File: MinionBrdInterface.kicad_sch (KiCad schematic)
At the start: 4 parts, among them J30 Backup Camera, J5 MinionConn, J6 SPI, SW1 BACKUP_SW

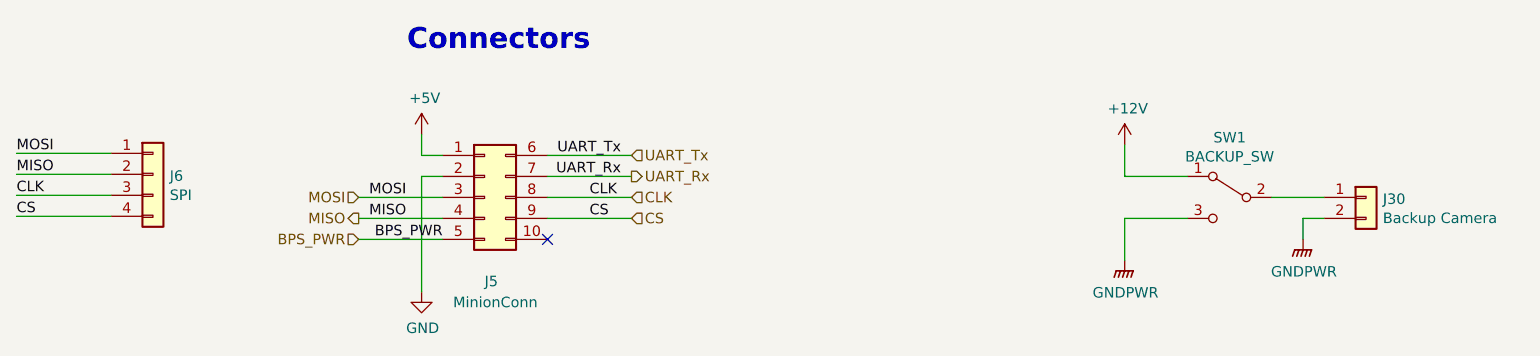
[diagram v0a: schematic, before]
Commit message: Schematic notations for rework changes
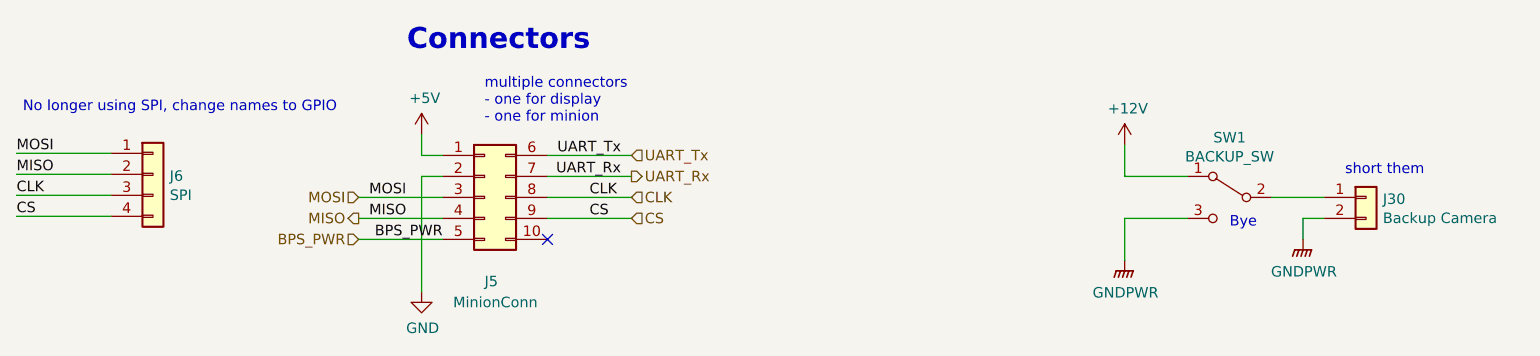
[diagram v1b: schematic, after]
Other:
- note added: "Bye"
- note added: "No longer using SPI, change names to GPIO"
- note added: "multiple connectors - one for display - one for minion"
- note added: "short them"

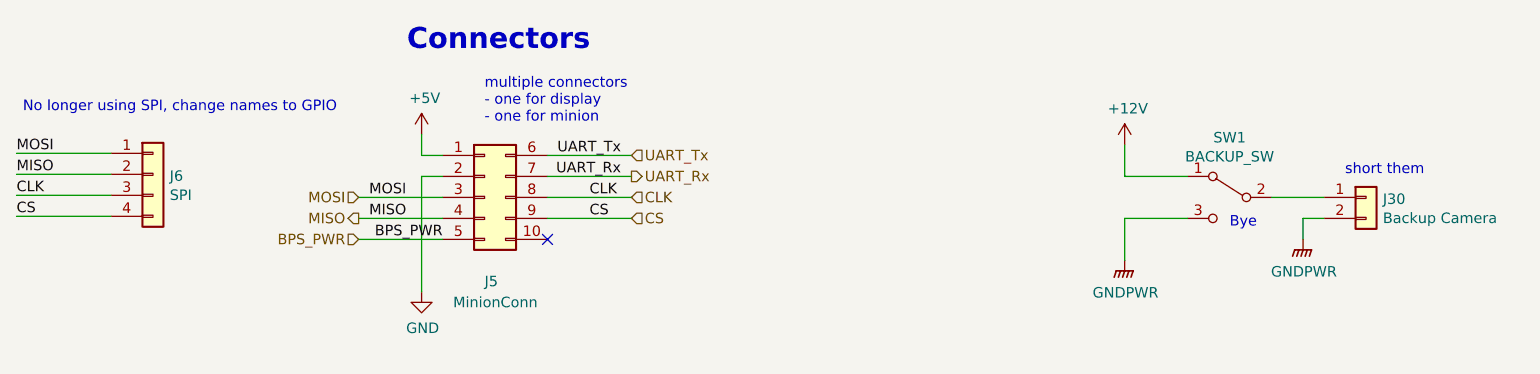
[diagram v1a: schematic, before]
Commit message: Updated schematic in accordance to previous weeks annotated changes
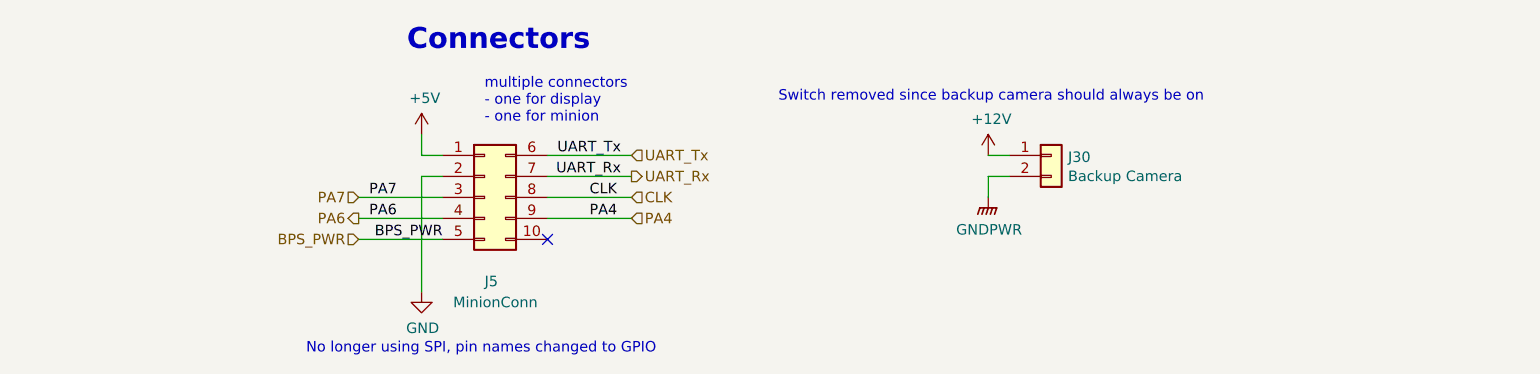
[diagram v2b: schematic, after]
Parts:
- removed J6: SPI, Connector_PinHeader_2.54mm:PinHeader_1x04_P2.54mm_Vertical, symbol Connector_Generic:Conn_01x04
- removed SW1: BACKUP_SW, Connector_Molex:Molex_Micro-Fit_3.0_43650-0315_1x03_P3.00mm_Vertical, symbol Switch:SW_SPDT
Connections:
- net +12V: now also J30.1 (Pin_1)
- net CS renamed PA4
- net MISO renamed PA6
- net MOSI renamed PA7
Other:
- note added: "No longer using SPI, pin names changed to GPIO"
- note added: "Switch removed since backup camera should always be on"
- note removed: "Bye"
- note removed: "No longer using SPI, change names to GPIO"
- note removed: "short them"
- moved on the sheet: J30

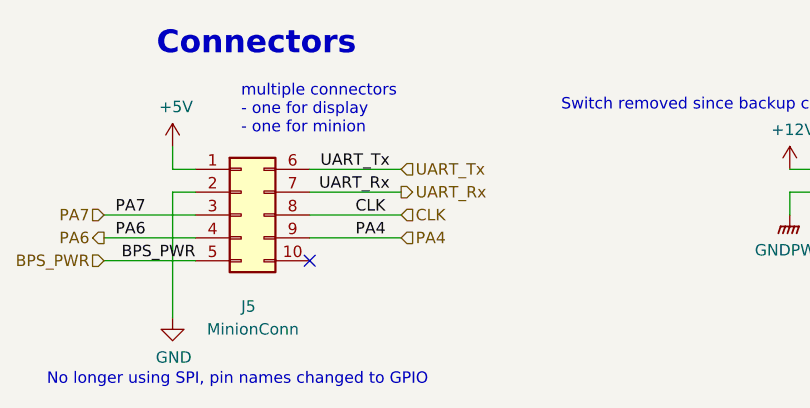
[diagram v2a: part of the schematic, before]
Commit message: Renamed Clk to PA5, removed CAN_TX/RX test points, deleted other .lck file and #auto_saved_files# (hopefully this does not break anything.
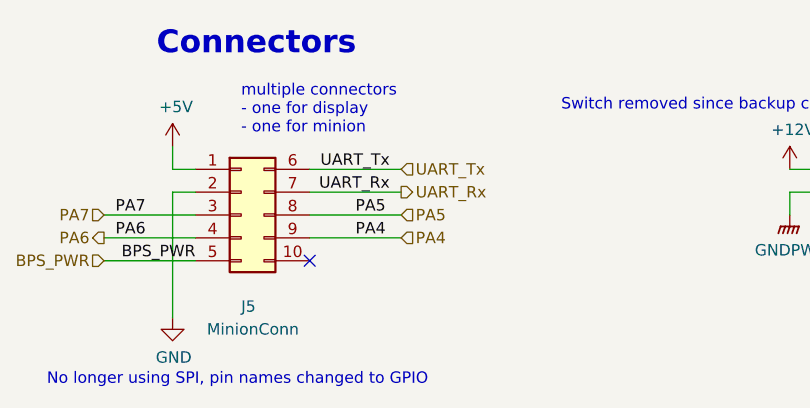
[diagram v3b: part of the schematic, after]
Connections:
- net CLK renamed PA5

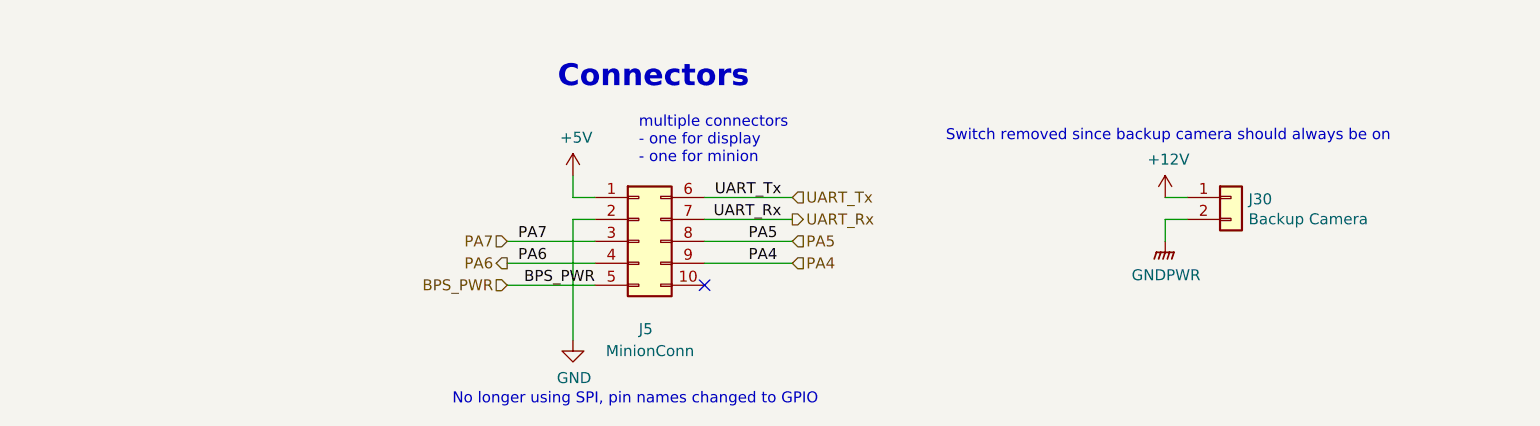
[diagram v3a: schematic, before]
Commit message: removed camera, fixed connectors, and changed status LEDS
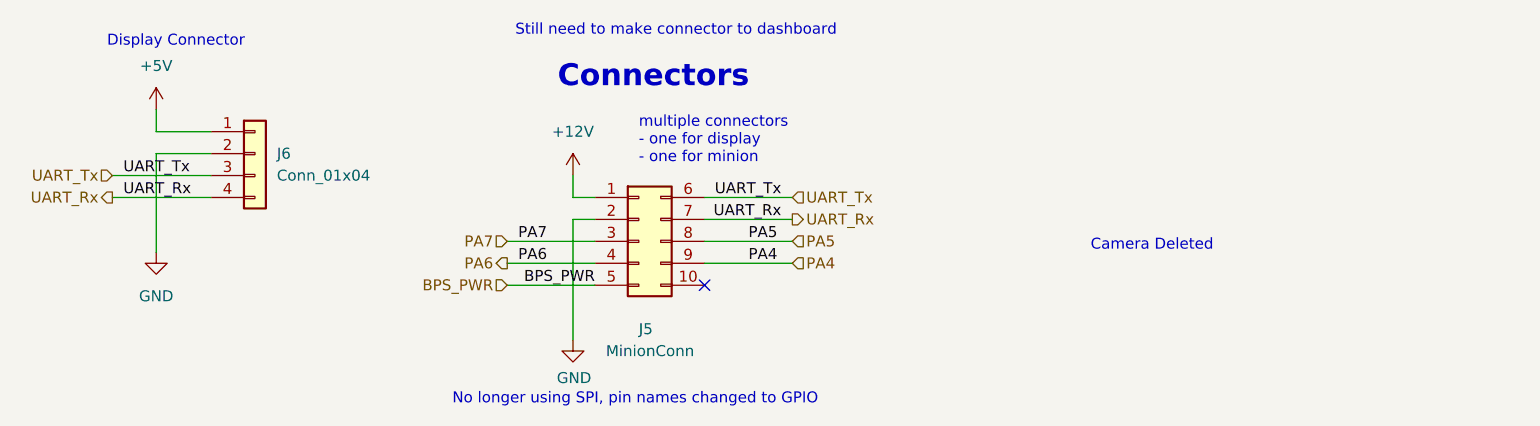
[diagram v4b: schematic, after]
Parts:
- removed J30: Backup Camera, Connector_Molex:Molex_Micro-Fit_3.0_43650-0215_1x02_P3.00mm_Vertical, symbol Connector_Generic:Conn_01x02
- added J6: Conn_01x04, Connector_Molex:Molex_Micro-Fit_3.0_43650-0415_1x04_P3.00mm_Vertical, symbol Connector_Generic:Conn_01x04
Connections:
- net +12V: now also J5.1 (Pin_1)
- net +5V: now also J6.1 (Pin_1); no longer J5.1 (Pin_1)
- net GND: now also J6.2 (Pin_2)
- net UART_Rx: now also J6.4 (Pin_4)
- net UART_Tx: now also J6.3 (Pin_3)
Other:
- note added: "Camera Deleted"
- note added: "Display Connector"
- note added: "Still need to make connector to dashboard"
- note removed: "Switch removed since backup camera should always be on"

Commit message: Schematic finished :) hopefully not broken
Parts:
- removed J5: MinionConn, Connector_Molex:Molex_Micro-Fit_3.0_43045-1012_2x05_P3.00mm_Vertical, symbol Connector_Generic:Conn_02x05_Top_Bottom
- added J4: Conn_02x05_Top_Bottom, symbol Connector_Generic:Conn_02x05_Top_Bottom
- added R10, R11, R12, R30, R33, R40, R5, R6: 4.9k, Resistor_SMD:R_0805_2012Metric, symbol Device:R_US
- added R32, R39, R41, R43, R45, R47, R49, R51: 510, Resistor_SMD:R_0805_2012Metric, symbol Device:R_US
- added U1, U16, U2, U20, U21, U22, U3, U4: EL3H7, Package_SO:SOP-4_4.4x2.6mm_P1.27mm, symbol Isolator:SFH617A-1
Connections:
- net +12V: now also J4.1 (Pin_1), U22.3
- net GND: now also R10.2, R11.2, R12.2, R30.2, R33.2, R5.2, R6.2, U22.2
- new net: R45.2, U16.1
- new net: R51.2, U22.1
- new net: R49.2, U21.1
- new net: R39.2, U2.1
- new net: R41.2, U3.1
- new net: R32.2, U1.1
- new net: R47.2, U20.1
- new net: R43.2, U4.1
- new net +3.3V: U1.3, U16.3, U2.3, U20.3, U21.3, U3.3, U4.3
- new net Cruise_En: J4.7 (Pin_7), R12.1, R47.1, U20.4
- new net Cruise_Set: J4.6 (Pin_6), R30.1, R49.1, U21.4
- new net Forward_Gear: J4.8 (Pin_8), R45.1
- new net Foward_Gear: R11.1, U16.4
- new net GNDPWR: J4.5 (Pin_5), R40.2, U1.2, U16.2, U2.2, U20.2, U21.2, U3.2, U4.2
- new net Heartbeat: J4.10 (Pin_10), R40.1, R51.1, U22.4
- new net IGN_1(Array): J4.3 (Pin_3), R33.1, R39.1, U2.4
- new net IGN_2(Motor): J4.4 (Pin_4), R32.1, R5.1, U1.4
- new net Regen: J4.2 (Pin_2), R41.1, R6.1, U3.4
- new net Reverse_Gear: J4.9 (Pin_9), R10.1, R43.1, U4.4
- no-connect marks 1 -> 0
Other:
- note added: "Connectors + Optoisolators"
- note removed: "Camera Deleted"
- note removed: "Connectors"
- note removed: "No longer using SPI, pin names changed to GPIO"
- note removed: "Still need to make connector to dashboard"
- note removed: "multiple connectors - one for display - one for minion"
- moved on the sheet: J6

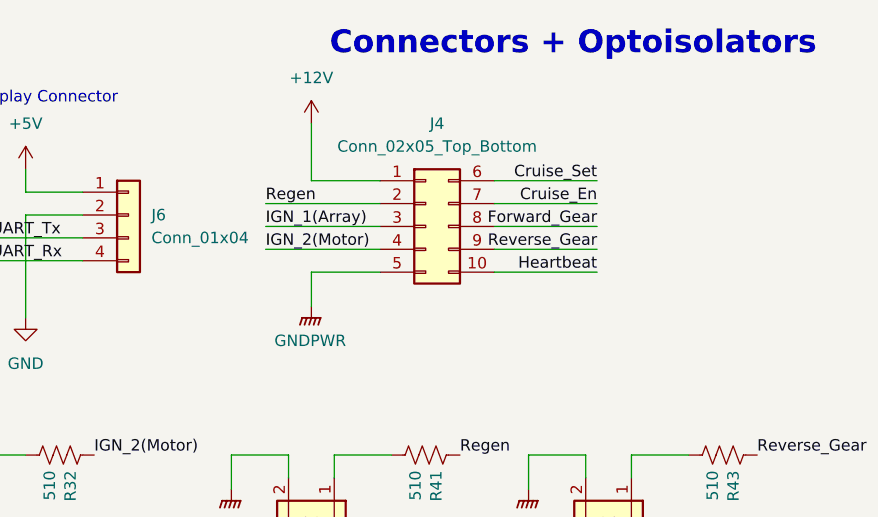
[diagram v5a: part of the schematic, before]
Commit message: Added back lights + drivers + timer for all blinkers and brake lights
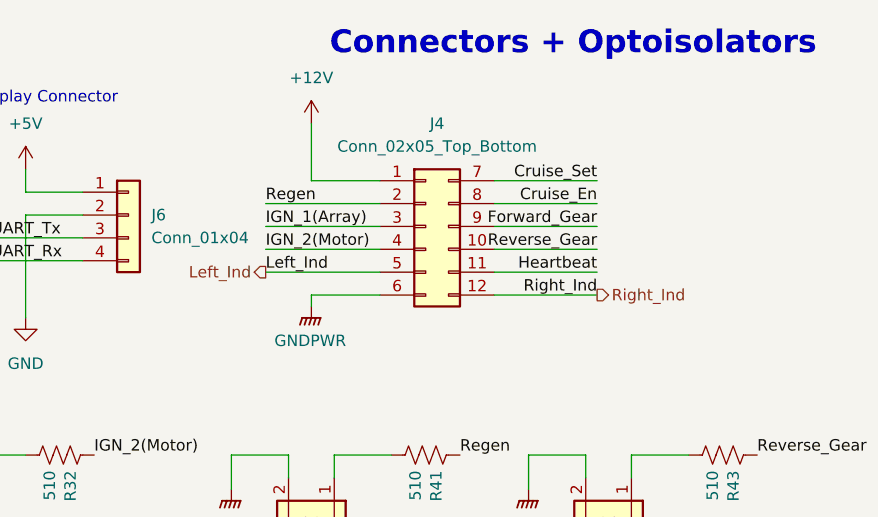
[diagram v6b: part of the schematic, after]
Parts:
- J4: symbol Connector_Generic:Conn_02x05_Top_Bottom -> Connector_Generic:Conn_02x06_Top_Bottom
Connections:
- net Cruise_En: now also J4.8 (Pin_8); no longer J4.7 (Pin_7)
- net Cruise_Set: now also J4.7 (Pin_7); no longer J4.6 (Pin_6)
- net Forward_Gear: now also J4.9 (Pin_9); no longer J4.8 (Pin_8)
- net GNDPWR: now also J4.6 (Pin_6); no longer J4.5 (Pin_5)
- net Heartbeat: now also J4.11 (Pin_11); no longer J4.10 (Pin_10)
- net Reverse_Gear: now also J4.10 (Pin_10); no longer J4.9 (Pin_9)
- new net Left_Ind: J4.5 (Pin_5)
- new net Right_Ind: J4.12 (Pin_12)
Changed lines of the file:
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@@
+	(wire
+		(pts
+			(xy 105.41 97.79) (xy 105.41 96.52)
+		)
+		(stroke
+			(width 0)
+			(type default)
+		)
+	)
 	(wire
 		(pts
@@
 	(wire
 		(pts
+			(xy 100.33 93.98) (xy 113.03 93.98)
+		)
+		(stroke
+			(width 0)
+			(type default)
+		)
+	)
+	(wire
+		(pts
 			(xy 144.78 144.78) (xy 152.4 144.78)
 		)
@@
 	(wire
 		(pts
-			(xy 105.41 93.98) (xy 113.03 93.98)
-		)
-		(stroke
-			(width 0)
-			(type default)
-		)
-	)
-	(wire
-		(pts
 			(xy 27.94 114.3) (xy 27.94 116.84)
 		)
@@
 	(wire
 		(pts
-			(xy 105.41 97.79) (xy 105.41 93.98)
+			(xy 105.41 96.52) (xy 113.03 96.52)
 		)
 		(stroke
@@
 		(pts
 			(xy 135.89 116.84) (xy 135.89 114.3)
+		)
+		(stroke
+			(width 0)
+			(type default)
+		)
+	)
+	(wire
+		(pts
+			(xy 125.73 96.52) (xy 137.16 96.52)
 		)
 		(stroke
@@
 		)
 	)
+	(label "Left_Ind"
+		(at 100.33 93.98 0)
+		(fields_autoplaced yes)
+		(effects
+			(font
+				(size 1.27 1.27)
+			)
+			(justify left bottom)
+		)
+	)
 	(label "Regen"
 		(at 100.33 86.36 0)
@@
 			)
 			(justify left bottom)
+		)
+	)
+	(label "Right_Ind"
+		(at 137.16 96.52 180)
+		(fields_autoplaced yes)
+		(effects
+			(font
+				(size 1.27 1.27)
+			)
+			(justify right bottom)
 		)
 	)
@@
 		)
 	)
+	(hierarchical_label "Left_Ind"
+		(shape output)
+		(at 100.33 93.98 180)
+		(fields_autoplaced yes)
+		(effects
+			(font
+				(size 1.27 1.27)
+			)
+			(justify right)
+		)
+	)
 	(hierarchical_label "Foward_Gear"
 		(shape output)
 		(at 193.04 144.78 0)
+		(fields_autoplaced yes)
+		(effects
+			(font
+				(size 1.27 1.27)
+			)
+			(justify left)
+		)
+	)
+	(hierarchical_label "Right_Ind"
+		(shape output)
+		(at 137.16 96.52 0)
 		(fields_autoplaced yes)
 		(effects
@@
 	)
 	(symbol
-		(lib_id "Connector_Generic:Conn_02x05_Top_Bottom")
+		(lib_id "Connector_Generic:Conn_02x06_Top_Bottom")
 		(at 118.11 88.9 0)
 		(unit 1)
@@
 			)
 		)
-		(property "Description" "Generic connector, double row, 02x05, top/bottom pin numbering scheme (row 1: 1...pins_per_row, row2: pins_per_row+1 ... num_pins), script generated (kicad-library-utils/schlib/autogen/connector/)"
+		(property "Description" "Generic connector, double row, 02x06, top/bottom pin numbering scheme (row 1: 1...pins_per_row, row2: pins_per_row+1 ... num_pins), script generated (kicad-library-utils/schlib/autogen/connector/)"
 			(at 118.11 88.9 0)
 			(effects
@@
 		(pin "1"
 		)
+		(pin "12"
+		)
+		(pin "11"
+		)
 		(instances
